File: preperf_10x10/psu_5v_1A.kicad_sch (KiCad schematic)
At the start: 8 parts, among them J2 Conn_01x02_Pin, U1 LM7805_TO220

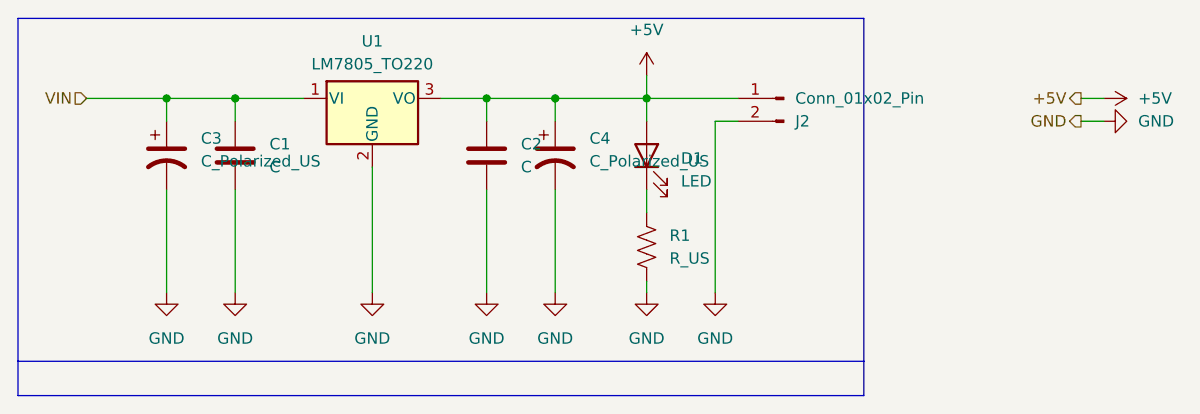
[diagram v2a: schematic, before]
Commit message: [ADD] Digital Logic Design project (FIUBA): PCB implementation of schmitt triggers, logic functions, counters, state machines, and logic probes
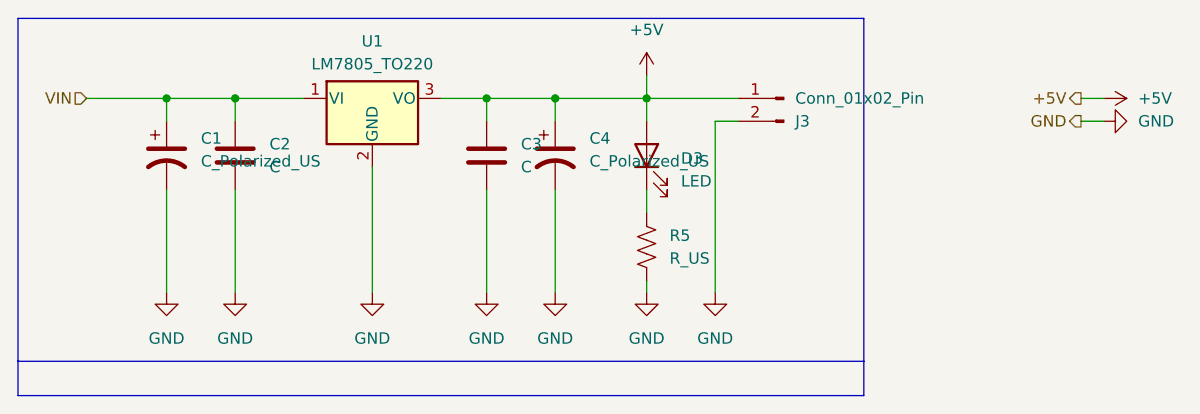
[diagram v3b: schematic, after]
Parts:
- renumbered C3 to C1, C1 to C2, C2 to C3, D1 to D3, J2 to J3, R1 to R5
